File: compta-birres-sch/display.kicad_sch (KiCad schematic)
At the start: 10 parts, among them U2 74HC595, U3 74HC595, U4 74HC595, U5 74HC595, U6 74HC595

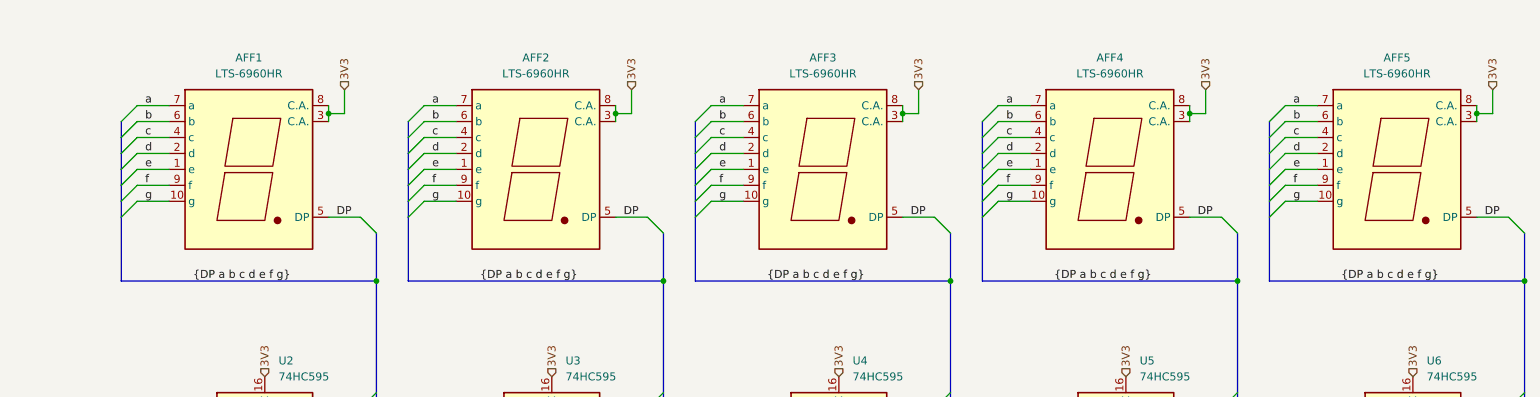
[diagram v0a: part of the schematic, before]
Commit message: Schematics: Updated the display schematics
Now we no longer have the simple 0.56" 7 Segment display, we've built
custom displays with led strips.
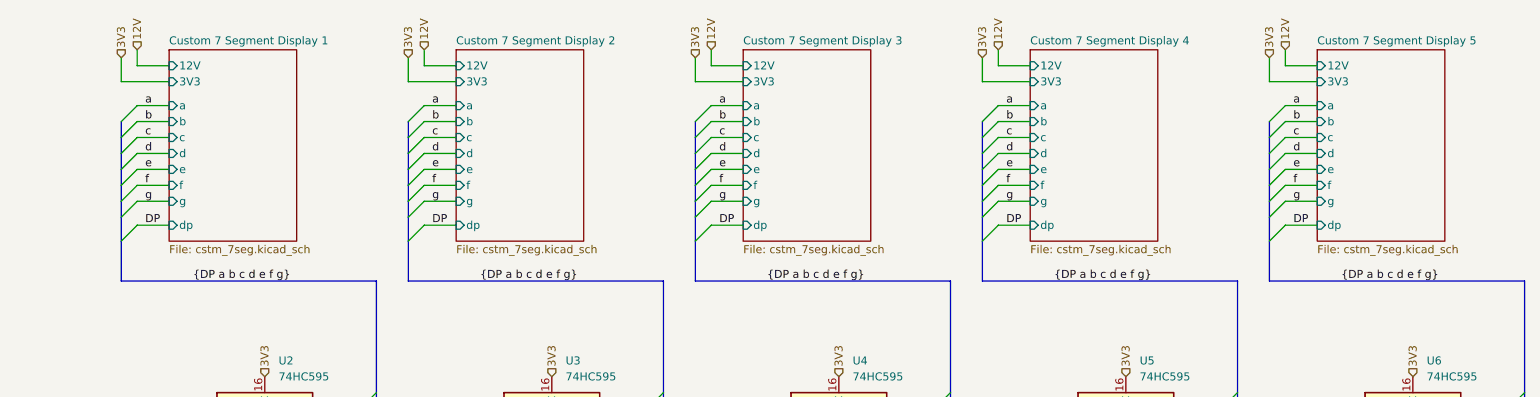
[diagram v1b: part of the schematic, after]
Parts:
- removed AFF1, AFF2, AFF3, AFF4, AFF5: LTS-6960HR, Display_7Segment:7SegmentLED_LTS6760_LTS6780, symbol Display_Character:LTS-6960HR
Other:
- added sheet Custom 7 Segment Display 1 (cstm_7seg.kicad_sch)
- added sheet Custom 7 Segment Display 2 (cstm_7seg.kicad_sch)
- added sheet Custom 7 Segment Display 3 (cstm_7seg.kicad_sch)
- added sheet Custom 7 Segment Display 4 (cstm_7seg.kicad_sch)
- added sheet Custom 7 Segment Display 5 (cstm_7seg.kicad_sch)
